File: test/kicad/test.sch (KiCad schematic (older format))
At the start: 5 parts

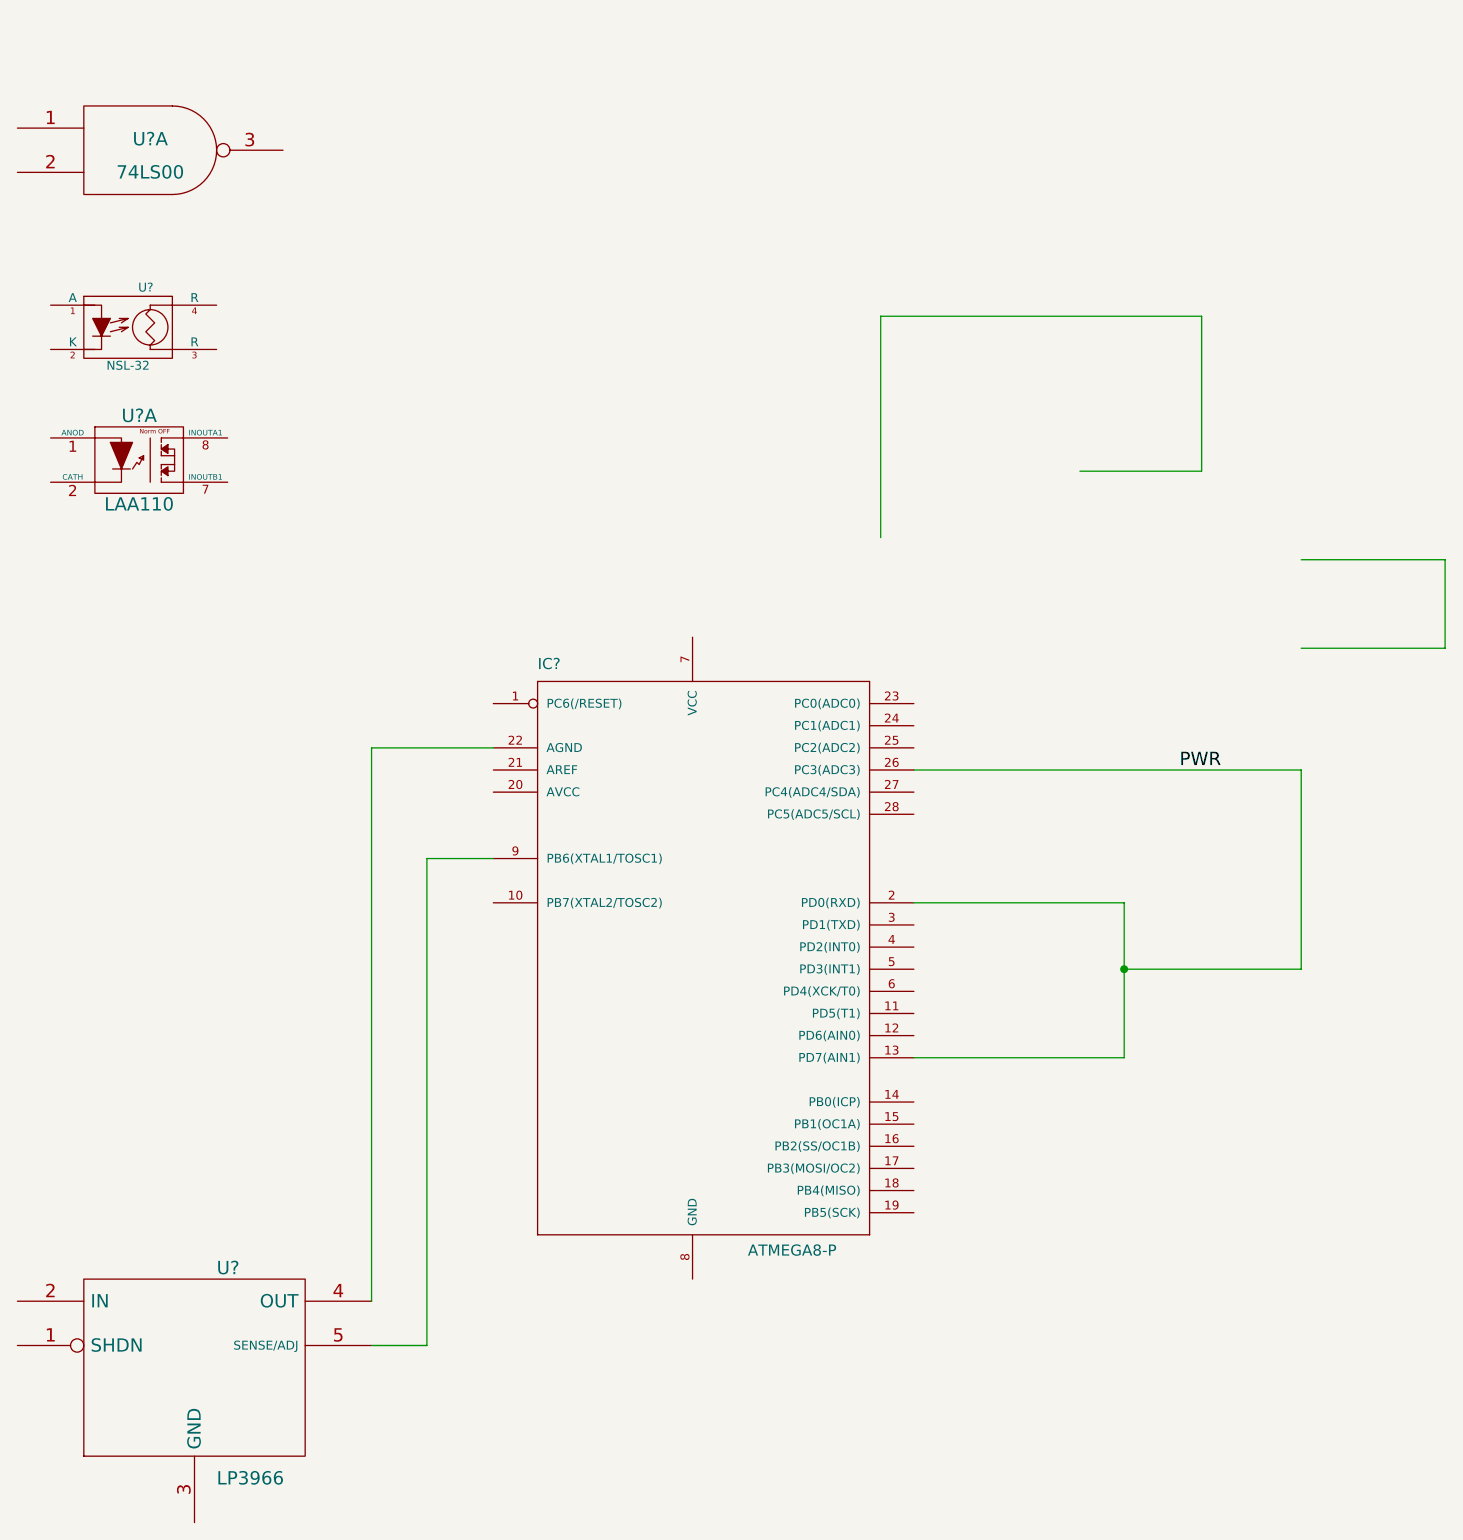
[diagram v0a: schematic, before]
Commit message: Parse and create the component instances in a kicad file.
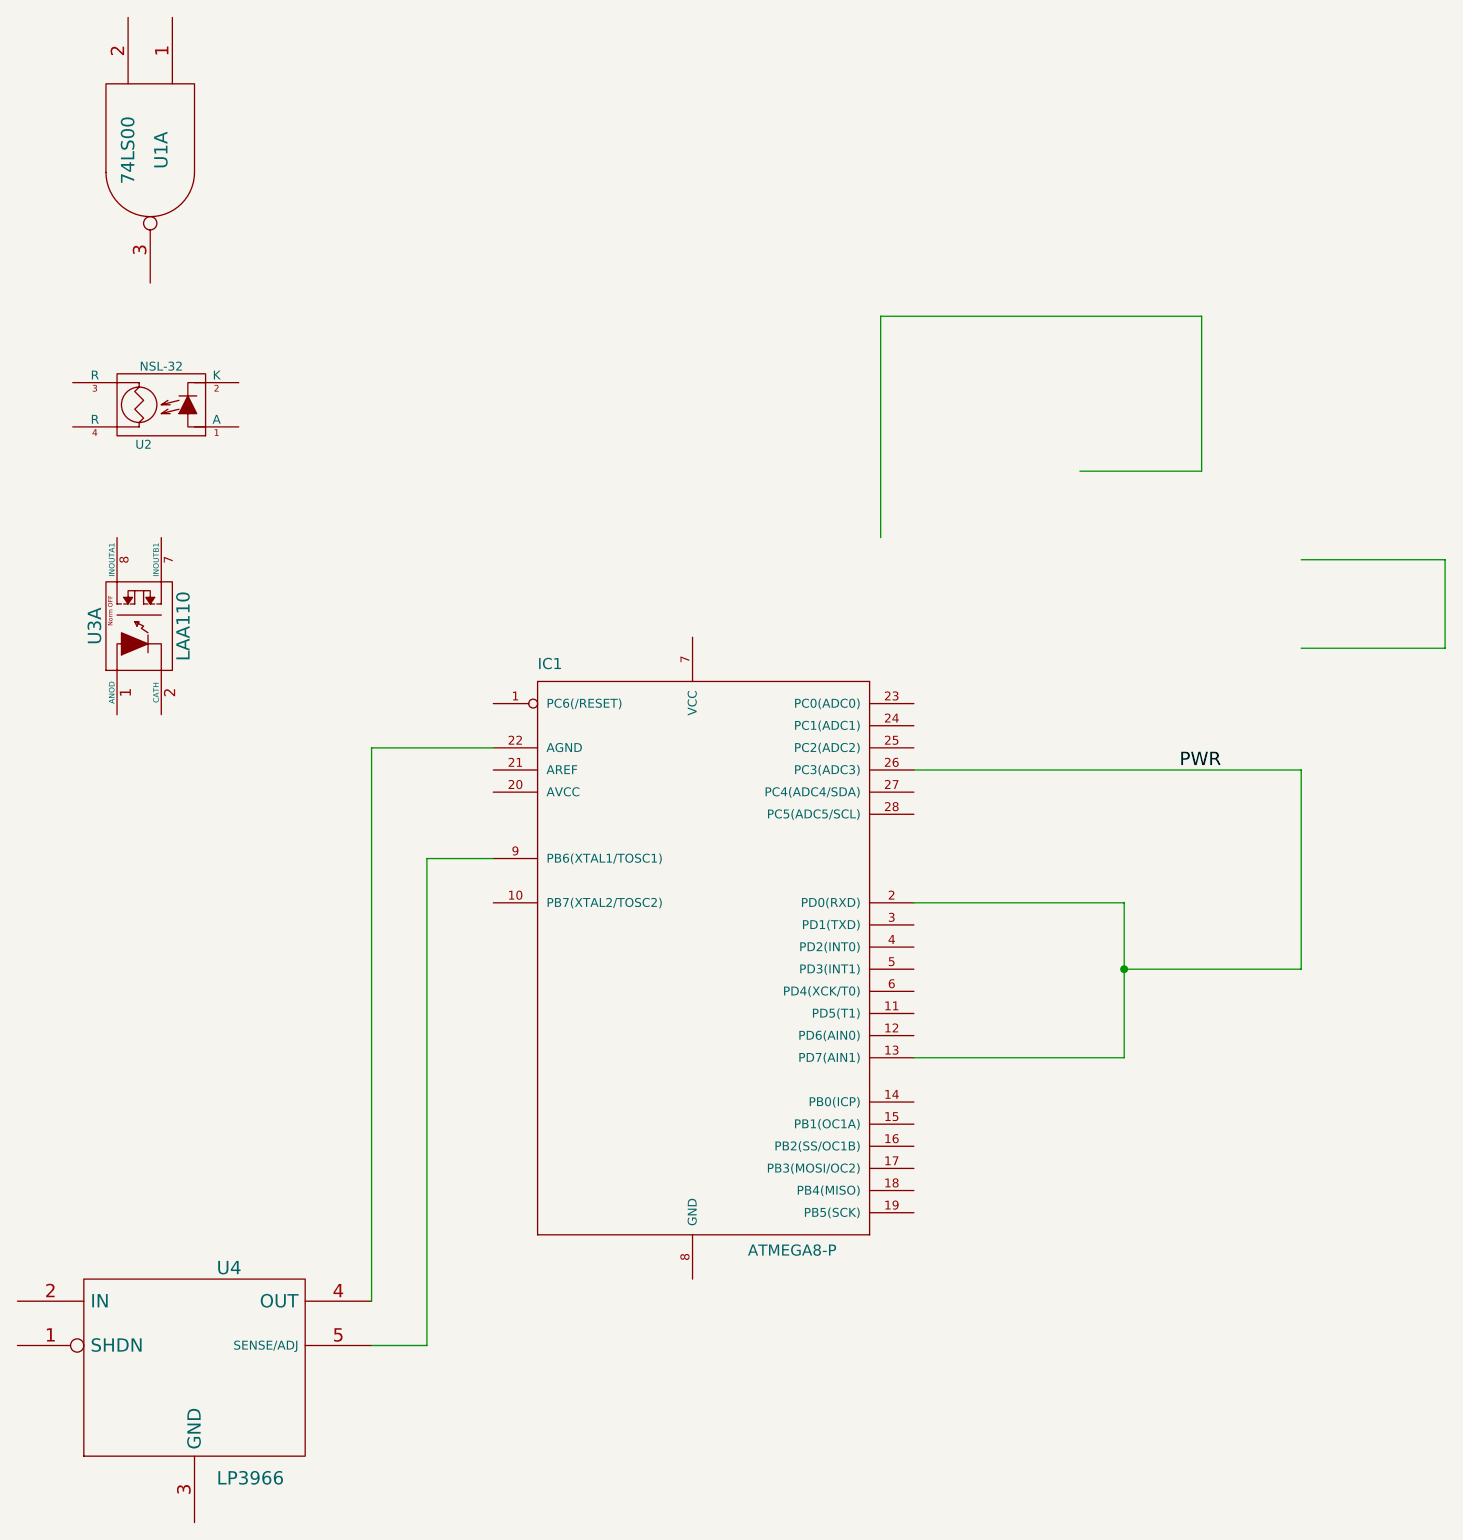
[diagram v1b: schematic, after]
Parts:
- gave numbers to parts that had none: 5
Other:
- moved on the sheet: U2, U3A
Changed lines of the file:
@@
-EESchema Schematic File Version 2  date Sun 11 Dec 2011 09:38:15 PM PST
+EESchema Schematic File Version 2  date Mon 12 Dec 2011 05:12:14 PM PST
 LIBS:power
 LIBS:device
@@
 Sheet 1 1
 Title ""
-Date "12 dec 2011"
+Date "13 dec 2011"
 Rev ""
 Comp ""
@@
 $EndDescr
 $Comp
-L LAA110 U?
+L LAA110 U3
 U 1 1 4EE59331
-P 1650 2650
-F 0 "U?" H 1650 2850 60  0000 C CNN
-F 1 "LAA110" H 1650 2450 60  0000 C CNN
-	1    1650 2650
-	1    0    0    -1
+P 1650 3400
+F 0 "U3" H 1650 3600 60  0000 C CNN
+F 1 "LAA110" H 1650 3200 60  0000 C CNN
+	1    1650 3400
+	0    -1   -1   0
 $EndComp
 $Comp
-L NSL-32 U?
+L NSL-32 U2
 U 1 1 4EE58F9A
-P 1600 2050
-F 0 "U?" H 1680 2230 40  0000 C CNN
-F 1 "NSL-32" H 1600 1877 40  0000 C CNN
-	1    1600 2050
-	1    0    0    -1
+P 1750 2400
+F 0 "U2" H 1830 2580 40  0000 C CNN
+F 1 "NSL-32" H 1750 2227 40  0000 C CNN
+	1    1750 2400
+	-1   0    0    1
 $EndComp
 $Comp
-L 74LS00 U?
+L 74LS00 U1
 U 1 1 4EE57ED5
 P 1700 1250
-F 0 "U?" H 1700 1300 60  0000 C CNN
+F 0 "U1" H 1700 1300 60  0000 C CNN
 F 1 "74LS00" H 1700 1150 60  0000 C CNN
 	1    1700 1250
-	1    0    0    -1
+	0    1    1    0
 $EndComp
 Wire Wire Line
@@
 PWR
 $Comp
-L LP3966 U?
+L LP3966 U4
 U 1 1 4E8E0625
 P 1900 6750
-F 0 "U?" H 2000 7200 60  0000 L CNN
+F 0 "U4" H 2000 7200 60  0000 L CNN
 F 1 "LP3966" H 2000 6250 60  0000 L CNN
 	1    1900 6750
@@
 $EndComp
 $Comp
-L ATMEGA8-P IC?
+L ATMEGA8-P IC1
 U 1 1 4E8DFDD4
 P 4150 4850
-F 0 "IC?" H 3450 6100 50  0000 L BNN
+F 0 "IC1" H 3450 6100 50  0000 L BNN
 F 1 "ATMEGA8-P" H 4400 3450 50  0000 L BNN
 F 2 "DIL28" H 4650 3375 50  0001 C CNN
